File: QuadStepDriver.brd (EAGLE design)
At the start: 100 x 50 mm, 124 parts, among them IC3 NCP1117ST50T3G, IC6 PIC18F4550_TQFP, U1 A4983, U2 A4983, U3 A4983, U4 A4983, X1 MSTBA4, X11 MSTBA4, X12 USB B, X14 ICSP-5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

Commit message: Just cleaning up the schematic
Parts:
- removed JP1: (no value), pinhead:1X10
- removed JP11: STAND-OFF, SparkFun:STAND-OFF
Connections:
- net N$65 renamed RA0
- net N$66 renamed RA1
- net N$67 renamed RA2
- net N$68 renamed RA3
- net N$69 renamed RA4
- net N$70 renamed RA5
- net N$71 renamed RE0
- net N$72 renamed RE1
- net N$74 renamed RC1
- net N$75 renamed RC2
- net N$76 renamed RC0
- net N$77 renamed RE2
- removed net N$56: JP1.2
- removed net N$57: JP1.3
- removed net N$58: JP1.4
- removed net N$59: JP1.5
- removed net N$60: JP1.6
- removed net N$61: JP1.7
- removed net N$62: JP1.8
- removed net N$63: JP1.9
- removed net N$64: JP1.10
- net LED1: no longer R33.2
- net N$55: now also R33.2; no longer JP1.1
- net PGC: no longer IC6.16
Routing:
- net PGC: track 19.3 -> 3.04 mm
- net LED1: track 4.81 -> 2.37 mm
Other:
- board text removed: "2-15-11"
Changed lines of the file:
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@@
 <board>
 <plain>
-<text x="-65.405" y="33.401" size="1.27" layer="16" font="vector" ratio="18" rot="MR270">2-15-11</text>
 <text x="7.5692" y="34.9758" size="0.508" layer="27" font="vector" ratio="7">Barrel Jack</text>
 <wire x1="100" y1="50" x2="0" y2="50" width="0" layer="20"/>
@@
 <element name="JP9" library="SparkFun" package="STAND-OFF" value="STAND-OFF" x="97.155" y="46.6725" smashed="yes" rot="R90"/>
 <element name="JP10" library="SparkFun" package="STAND-OFF" value="STAND-OFF" x="50.165" y="11.43" smashed="yes" rot="R90"/>
-<element name="JP11" library="SparkFun" package="STAND-OFF" value="STAND-OFF" x="-69.85" y="2.54" smashed="yes" rot="R90"/>
 <element name="JP12" library="SparkFun" package="STAND-OFF" value="STAND-OFF" x="3.175" y="46.6725" smashed="yes" rot="R90"/>
 <element name="U3" library="SparkFun" package="QFN-28-5MM" value="A4983" x="12.7" y="17.145" smashed="yes" rot="R180">
@@
 <attribute name="OC_FARNELL" value="3705195" x="81.915" y="45.4025" size="1.778" layer="27" rot="R180" display="off"/>
 </element>
-<element name="JP1" library="pinhead" package="1X10" value="" x="1.27" y="63.5"/>
 <element name="X12" library="con-berg" package="PN61729" value="USB B" x="13.97" y="39.6875" rot="R180">
 <attribute name="OC_NEWARK" value="unknown" x="29.845" y="20.6375" size="1.778" layer="27" rot="R180" display="off"/>
@@
 </signal>
 <signal name="LED1">
-<contactref element="R33" pad="2"/>
 <contactref element="IC6" pad="14"/>
 <wire x1="49.615" y1="35.3825" x2="51.9825" y2="35.3825" width="0.3048" layer="1"/>
-<wire x1="51.9825" y1="35.3825" x2="53.71" y2="33.655" width="0.3048" layer="1"/>
 </signal>
 <signal name="PGD">
@@
 <signal name="PGC">
 <contactref element="X14" pad="5"/>
-<contactref element="IC6" pad="16"/>
-<wire x1="49.615" y1="36.9825" x2="65.875" y2="36.9825" width="0.254" layer="1"/>
 <wire x1="65.875" y1="36.9825" x2="66.675" y2="37.7825" width="0.254" layer="1"/>
 <wire x1="66.675" y1="37.7825" x2="68.58" y2="37.7825" width="0.254" layer="1"/>
@@
 <wire x1="80.0125" y1="25.2975" x2="79.66" y2="25.2625" width="0.254" layer="1"/>
 </signal>
-<signal name="N$55">
-<contactref element="JP1" pad="1"/>
-</signal>
-<signal name="N$56">
-<contactref element="JP1" pad="2"/>
-</signal>
-<signal name="N$57">
-<contactref element="JP1" pad="3"/>
-</signal>
-<signal name="N$58">
-<contactref element="JP1" pad="4"/>
-</signal>
-<signal name="N$59">
-<contactref element="JP1" pad="5"/>
-</signal>
-<signal name="N$60">
-<contactref element="JP1" pad="6"/>
-</signal>
-<signal name="N$61">
-<contactref element="JP1" pad="7"/>
-</signal>
-<signal name="N$62">
-<contactref element="JP1" pad="8"/>
-</signal>
-<signal name="N$63">
-<contactref element="JP1" pad="9"/>
-</signal>
-<signal name="N$64">
-<contactref element="JP1" pad="10"/>
-</signal>
-<signal name="N$65">
+<signal name="RA0">
 <contactref element="IC6" pad="19"/>
 <contactref element="JP5" pad="8"/>
@@
 <wire x1="49.615" y1="39.3825" x2="56.21" y2="39.3825" width="0.3048" layer="1"/>
 </signal>
-<signal name="N$66">
+<signal name="RA1">
 <contactref element="IC6" pad="20"/>
 <contactref element="JP5" pad="7"/>
@@
 <wire x1="59.69" y1="44.1325" x2="59.69" y2="45.4025" width="0.3048" layer="1"/>
 </signal>
-<signal name="N$67">
+<signal name="RA2">
 <contactref element="IC6" pad="21"/>
 <contactref element="JP5" pad="6"/>
@@
 <wire x1="49.64" y1="40.9575" x2="49.615" y2="40.9825" width="0.3048" layer="1"/>
 </signal>
-<signal name="N$68">
+<signal name="RA3">
 <contactref element="IC6" pad="22"/>
 <contactref element="JP5" pad="5"/>
@@
 <wire x1="57.15" y1="44.1325" x2="57.15" y2="45.4025" width="0.3048" layer="1"/>
 </signal>
-<signal name="N$69">
+<signal name="RA4">
 <contactref element="IC6" pad="23"/>
 <contactref element="JP5" pad="3"/>
@@
 <wire x1="54.61" y1="44.1325" x2="54.61" y2="45.4025" width="0.3048" layer="1"/>
 </signal>
-<signal name="N$70">
+<signal name="RA5">
 <contactref element="IC6" pad="24"/>
 <contactref element="JP5" pad="4"/>
@@
 <wire x1="55.88" y1="46.6725" x2="54.61" y2="47.9425" width="0.3048" layer="1"/>
 </signal>
-<signal name="N$71">
+<signal name="RE0">
 <contactref element="IC6" pad="25"/>
 <contactref element="JP5" pad="1"/>
@@
 <wire x1="51.435" y1="44.7675" x2="52.07" y2="45.4025" width="0.3048" layer="1"/>
 </signal>
-<signal name="N$72">
+<signal name="RE1">
 <contactref element="IC6" pad="26"/>
 <contactref element="JP5" pad="2"/>
@@
 <wire x1="57.37" y1="31.75" x2="55.51" y2="31.75" width="0.3048" layer="1"/>
 </signal>
-<signal name="N$74">
+<signal name="RC1">
 <contactref element="IC6" pad="35"/>
 <contactref element="JP2" pad="2"/>
@@
 <wire x1="31.115" y1="43.18" x2="31.115" y2="44.45" width="0.3048" layer="1"/>
 </signal>
-<signal name="N$75">
+<signal name="RC2">
 <contactref element="IC6" pad="36"/>
 <contactref element="JP2" pad="4"/>
@@
 <wire x1="32.8425" y1="40.1825" x2="28.575" y2="44.45" width="0.3048" layer="1"/>
 </signal>
-<signal name="N$76">
+<signal name="RC0">
 <contactref element="IC6" pad="32"/>
 <contactref element="JP2" pad="3"/>
@@
 <wire x1="29.845" y1="45.72" x2="28.575" y2="46.99" width="0.3048" layer="1"/>
 </signal>
-<signal name="N$77">
+<signal name="RE2">
 <contactref element="IC6" pad="27"/>
 <contactref element="JP2" pad="1"/>
@@
 <wire x1="39.6875" y1="46.99" x2="31.115" y2="46.99" width="0.3048" layer="16"/>
 </signal>
+<signal name="N$55">
+<contactref element="R33" pad="2"/>
+</signal>
 </signals>
-<errors>
-</errors>
 </board>
 </drawing>

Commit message: PCB: Finalizando Gerbers
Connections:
- removed net N$55: R33.2
- net LED1: now also IC6.15, R34.2; no longer IC6.14
- net LED2: now also IC6.14, R33.2; no longer IC6.15, R34.2
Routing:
- net LED1: track 2.37 -> 4.35 mm
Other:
- board text added: "1"
- board text added: "2"
- board text added: "3"
- board text added: "4"
- board text added: "DIR"
- board text added: "EN"
- board text added: "ICSP"
- board text added: "LED1"
- board text added: "LED2"
- board text added: "MS1"
- board text added: "MS2"
- board text added: "MS3"
- board text added: "POWER"
- board text added: "RST"
- board text added: "SLP"
- board text added: "STEP"
- board text added: "USB"

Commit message: Changing some components values, and organizing component values placement
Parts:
- R33, R34, R35: value 10k -> 330R
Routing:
- net VCC: track 276.1 -> 279.2 mm

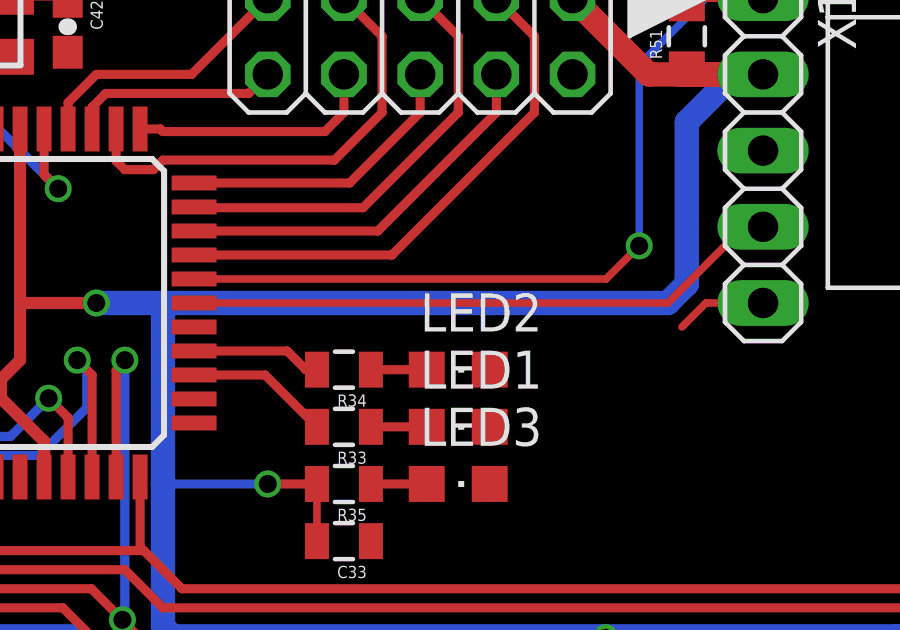
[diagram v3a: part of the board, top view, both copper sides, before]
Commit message: Fixing some unconneted routes from board REV1.
PGC and power input GND are now connected.
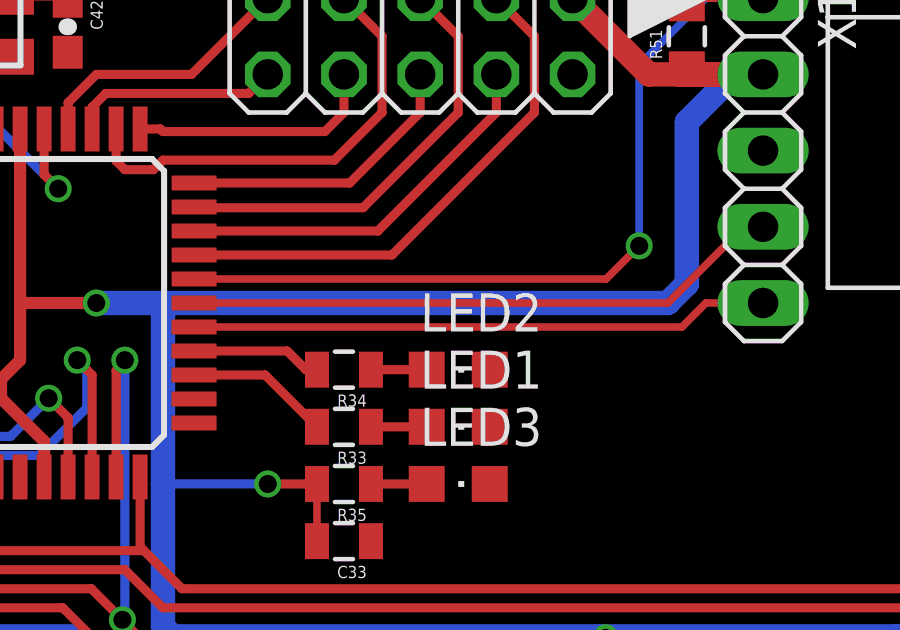
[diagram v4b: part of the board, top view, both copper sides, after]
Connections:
- net GND: now also X11.3, X11.4
- net PGC: now also IC6.16
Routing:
- net PGC: track 3.04 -> 19.3 mm
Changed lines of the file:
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@@
 <contactref element="LED3" pad="C"/>
 <contactref element="JP2" pad="5"/>
+<contactref element="X11" pad="3"/>
+<contactref element="X11" pad="4"/>
 </signal>
 <signal name="N$1">
@@
 </signal>
 <signal name="PGC">
+<contactref element="IC6" pad="16"/>
 <contactref element="X14" pad="5"/>
-<wire x1="65.875" y1="36.9825" x2="66.675" y2="37.7825" width="0.254" layer="1"/>
+<wire x1="66.3575" y1="37.465" x2="66.675" y2="37.7825" width="0.254" layer="1"/>
 <wire x1="66.675" y1="37.7825" x2="68.58" y2="37.7825" width="0.254" layer="1"/>
+<wire x1="49.615" y1="36.9825" x2="65.875" y2="36.9825" width="0.254" layer="1"/>
+<wire x1="65.875" y1="36.9825" x2="66.3575" y2="37.465" width="0.254" layer="1"/>
 </signal>
 <signal name="VBUS">
